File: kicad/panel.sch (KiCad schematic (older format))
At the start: 12 parts, among them CON21 CON5x2, CON22 CON5x2, SW1 SW_PUSH

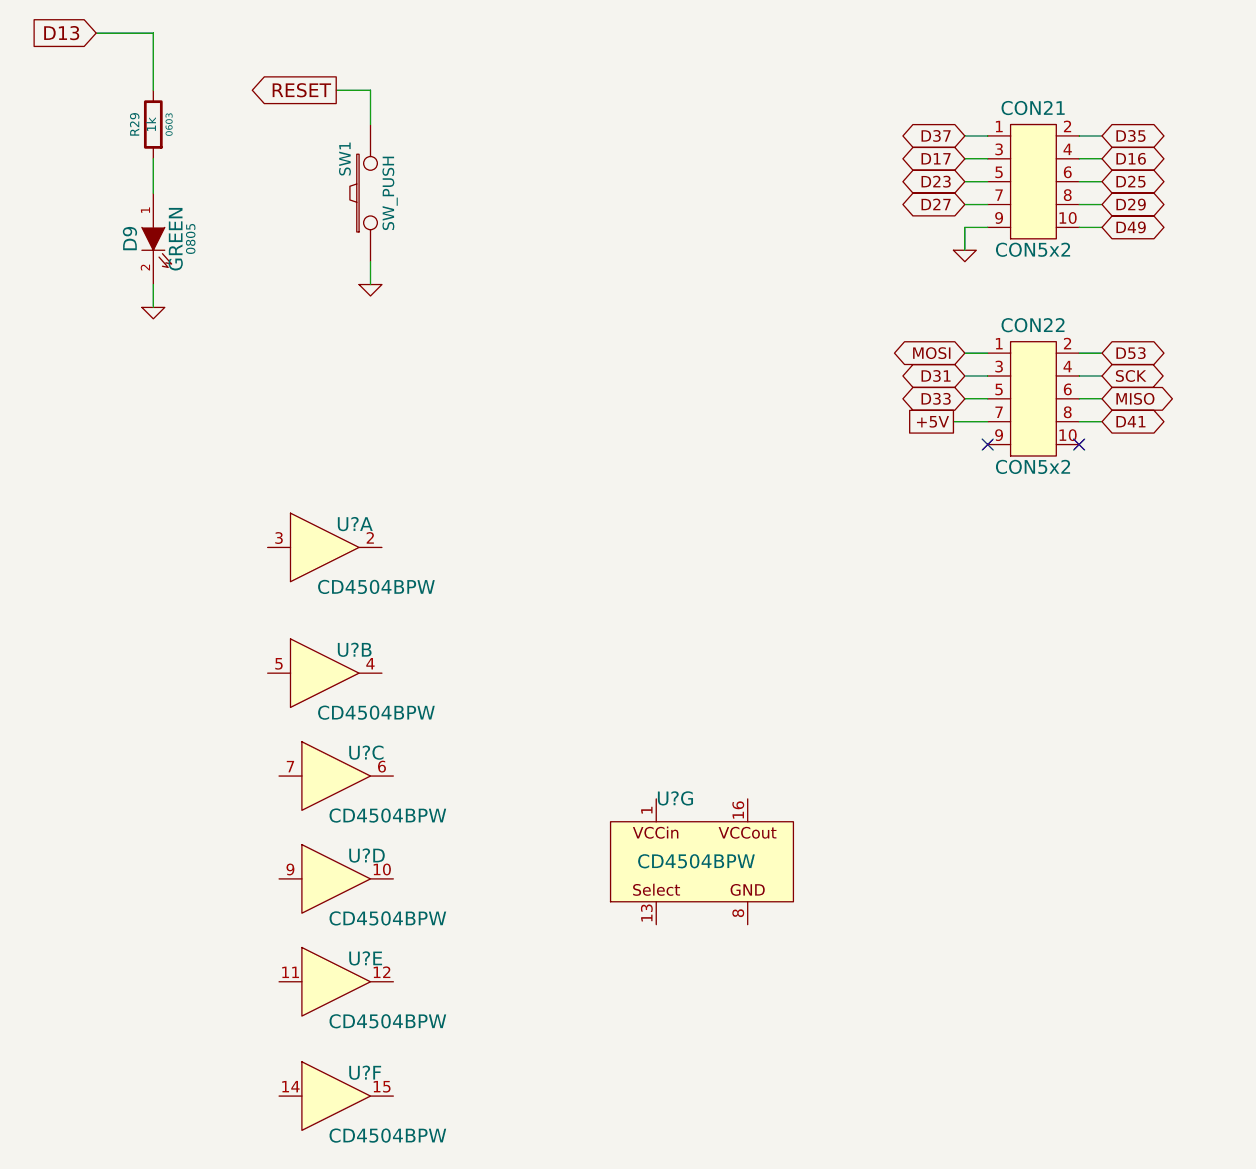
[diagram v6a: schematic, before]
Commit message: Add translators for LCD
ref #11
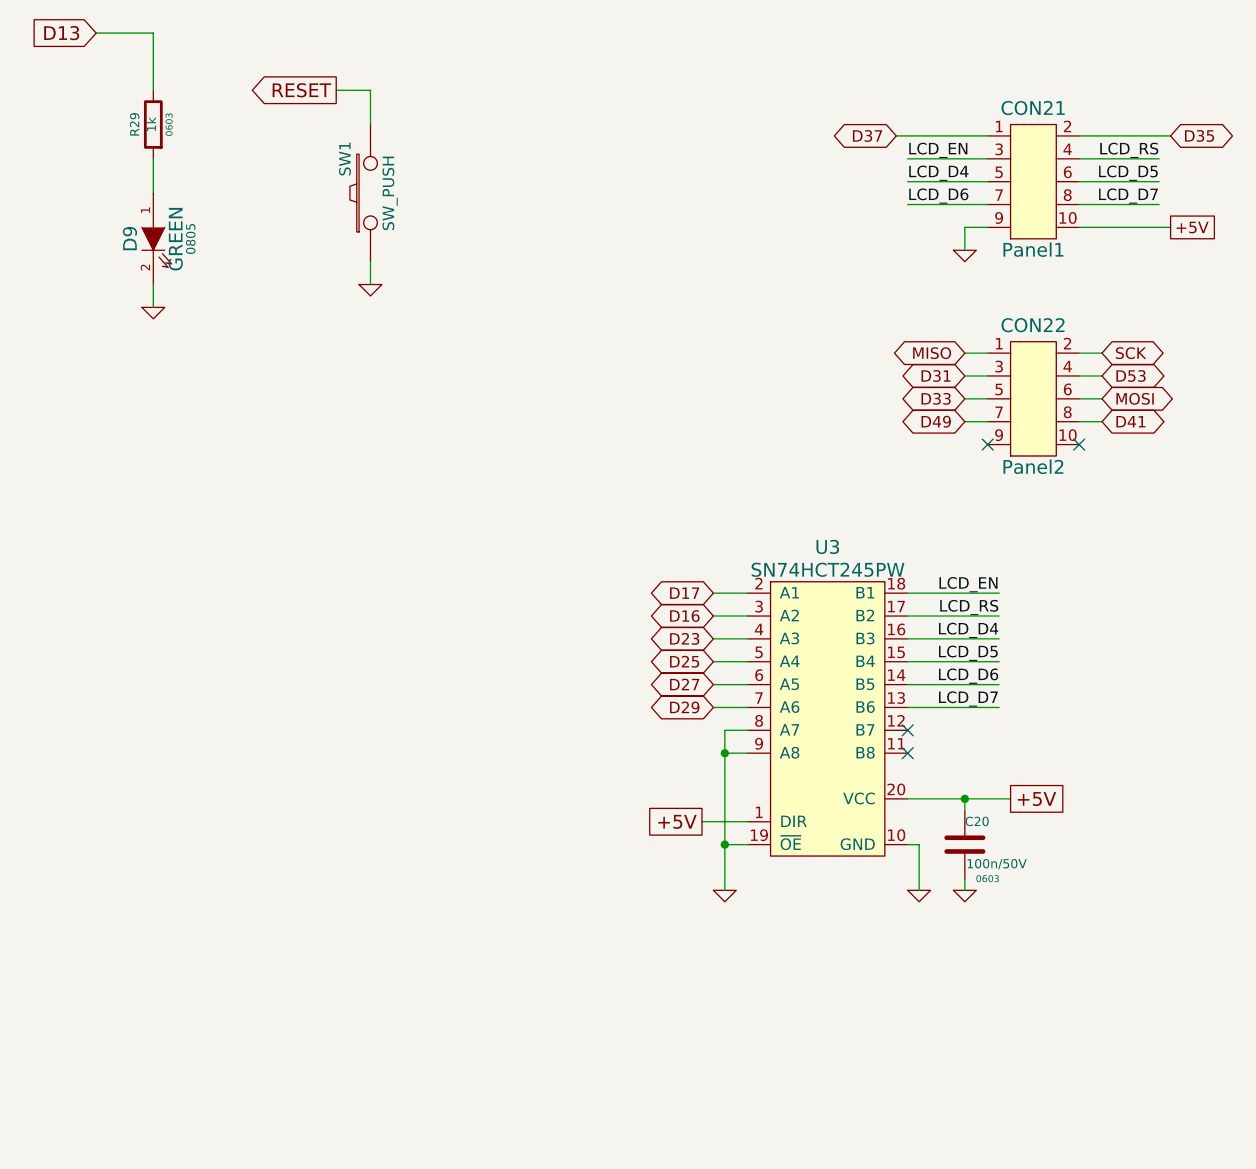
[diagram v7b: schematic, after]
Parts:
- removed U? (x7): CD4504BPW, TSSOP16, symbol CD4504BPW
- added C20: 100n/50V, 0603, symbol C
- added U3: SN74HCT245PW, symbol SN74HCT245PW
- CON21: value CON5x2 -> Panel1
- CON22: value CON5x2 -> Panel2
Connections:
- net +5V: now also CON21.10, C20.1, U3.1 (DIR), U3.20 (VCC); no longer CON22.7
- net D16: now also U3.3 (A2); no longer CON21.4
- net D17: now also U3.2 (A1); no longer CON21.3
- net D23: now also U3.4 (A3); no longer CON21.5
- net D25: now also U3.5 (A4); no longer CON21.6
- net D27: now also U3.6 (A5); no longer CON21.7
- net D29: now also U3.7 (A6); no longer CON21.8
- net D49: now also CON22.7; no longer CON21.10
- net D53: now also CON22.4; no longer CON22.2
- net GND: now also C20.2, U3.10 (GND), U3.19 (~OE), U3.8 (A7), U3.9 (A8)
- net MISO: now also CON22.1; no longer CON22.6
- net MOSI: now also CON22.6; no longer CON22.1
- net SCK: now also CON22.2; no longer CON22.4
- new net LCD_D4: CON21.5, U3.16 (B3)
- new net LCD_D5: CON21.6, U3.15 (B4)
- new net LCD_D6: CON21.7, U3.14 (B5)
- new net LCD_D7: CON21.8, U3.13 (B6)
- new net LCD_EN: CON21.3, U3.18 (B1)
- new net LCD_RS: CON21.4, U3.17 (B2)
- no-connect marks 2 -> 4
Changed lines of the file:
@@
 	0    -1   1    0
 $EndComp
-Text GLabel 6150 1500 2    50   BiDi ~ 0
+Text GLabel 6450 1500 2    50   BiDi ~ 0
 D35
-Text GLabel 5550 1500 0    50   BiDi ~ 0
+Text GLabel 5250 1500 0    50   BiDi ~ 0
 D37
 $Comp
@@
 P 5850 1700
 F 0 "CON21" H 5850 2020 60  0000 C CNN
-F 1 "CON5x2" H 5850 1400 60  0000 C CNN
+F 1 "Panel1" H 5850 1400 60  0000 C CNN
 F 2 "" H 5850 1700 40  0000 C CNN
 F 3 "" H 5850 1700 40  0000 C CNN
@@
 P 5850 2650
 F 0 "CON22" H 5850 2970 60  0000 C CNN
-F 1 "CON5x2" H 5850 2350 60  0000 C CNN
+F 1 "Panel2" H 5850 2350 60  0000 C CNN
 F 2 "" H 5850 2650 40  0000 C CNN
 F 3 "" H 5850 2650 40  0000 C CNN
@@
 	1    0    0    -1
 $EndComp
-Text GLabel 5550 1600 0    50   BiDi ~ 0
+Text GLabel 4450 3500 0    50   BiDi ~ 0
 D17
-Text GLabel 5550 1700 0    50   BiDi ~ 0
+Text GLabel 4450 3700 0    50   BiDi ~ 0
 D23
-Text GLabel 5550 1800 0    50   BiDi ~ 0
+Text GLabel 4450 3900 0    50   BiDi ~ 0
 D27
-Text GLabel 6150 1600 2    50   BiDi ~ 0
+Text GLabel 4450 3600 0    50   BiDi ~ 0
 D16
-Text GLabel 6150 1700 2    50   BiDi ~ 0
+Text GLabel 4450 3800 0    50   BiDi ~ 0
 D25
-Text GLabel 6150 1800 2    50   BiDi ~ 0
+Text GLabel 4450 4000 0    50   BiDi ~ 0
 D29
-Text GLabel 6150 1900 2    50   BiDi ~ 0
-D49
 Wire Wire Line
 	2000 1750 2000 1600
@@
 	2950 2150 2950 2050
 Wire Wire Line
-	6150 1500 6050 1500
-Wire Wire Line
-	6050 1600 6150 1600
-Wire Wire Line
-	6150 1700 6050 1700
-Wire Wire Line
-	6050 1800 6150 1800
-Wire Wire Line
-	6150 1900 6050 1900
+	6450 1500 6050 1500
+Wire Wire Line
+	6050 1600 6400 1600
+Wire Wire Line
+	6400 1700 6050 1700
+Wire Wire Line
+	6050 1800 6400 1800
+Wire Wire Line
+	6450 1900 6050 1900
 Wire Wire Line
 	5550 1900 5650 1900
 Wire Wire Line
-	5550 1800 5650 1800
-Wire Wire Line
-	5550 1700 5650 1700
-Wire Wire Line
-	5650 1600 5550 1600
-Wire Wire Line
-	5650 1500 5550 1500
+	5300 1800 5650 1800
+Wire Wire Line
+	5300 1700 5650 1700
+Wire Wire Line
+	5650 1600 5300 1600
+Wire Wire Line
+	5650 1500 5250 1500
 $Comp
 L GND #PWR52
@@
 Wire Wire Line
 	5550 1900 5550 2000
-Text GLabel 5550 2450 0    50   BiDi ~ 0
+Text GLabel 6150 2650 2    50   BiDi ~ 0
 MOSI
 Text GLabel 5550 2550 0    50   BiDi ~ 0
@@
 Text GLabel 5550 2650 0    50   BiDi ~ 0
 D33
-Text GLabel 5500 2750 0    50   UnSpc ~ 0
+Text GLabel 6450 1900 2    50   UnSpc ~ 0
 +5V
 Wire Wire Line
-	5500 2750 5650 2750
+	5550 2750 5650 2750
 Wire Wire Line
 	5550 2650 5650 2650
@@
 Wire Wire Line
 	5650 2450 5550 2450
+Text GLabel 6150 2550 2    50   BiDi ~ 0
+D53
 Text GLabel 6150 2450 2    50   BiDi ~ 0
-D53
-Text GLabel 6150 2550 2    50   BiDi ~ 0
 SCK
-Text GLabel 6150 2650 2    50   BiDi ~ 0
+Text GLabel 5550 2450 0    50   BiDi ~ 0
 MISO
 Text GLabel 6150 2750 2    50   BiDi ~ 0
@@
 NoConn ~ 6050 2850
 NoConn ~ 5650 2850
-$Comp
-L CD4504BPW U?
-U 1 1 538D7C6B
-P 2750 3300
-F 0 "U?" H 2800 3400 60  0000 L CNN
-F 1 "CD4504BPW" H 2975 3125 60  0000 C CNN
-F 2 "TSSOP16" H 2625 3300 40  0001 L CNN
-F 3 "" H 2600 3900 60  0001 L CNN
-	1    2750 3300
-	1    0    0    -1
-$EndComp
-$Comp
-L CD4504BPW U?
-U 2 1 538D7CB8
-P 2750 3850
-F 0 "U?" H 2800 3950 60  0000 L CNN
-F 1 "CD4504BPW" H 2975 3675 60  0000 C CNN
-F 2 "TSSOP16" H 2625 3850 40  0001 L CNN
-F 3 "" H 2600 4450 60  0001 L CNN
-	2    2750 3850
-	1    0    0    -1
-$EndComp
-$Comp
-L CD4504BPW U?
-U 3 1 538D7D0D
-P 2800 4300
-F 0 "U?" H 2850 4400 60  0000 L CNN
-F 1 "CD4504BPW" H 3025 4125 60  0000 C CNN
-F 2 "TSSOP16" H 2675 4300 40  0001 L CNN
-F 3 "" H 2650 4900 60  0001 L CNN
-	3    2800 4300
-	1    0    0    -1
-$EndComp
-$Comp
-L CD4504BPW U?
-U 4 1 538D7D48
-P 2800 4750
-F 0 "U?" H 2850 4850 60  0000 L CNN
-F 1 "CD4504BPW" H 3025 4575 60  0000 C CNN
-F 2 "TSSOP16" H 2675 4750 40  0001 L CNN
-F 3 "" H 2650 5350 60  0001 L CNN
-	4    2800 4750
-	1    0    0    -1
-$EndComp
-$Comp
-L CD4504BPW U?
-U 5 1 538D7D79
-P 2800 5200
-F 0 "U?" H 2850 5300 60  0000 L CNN
-F 1 "CD4504BPW" H 3025 5025 60  0000 C CNN
-F 2 "TSSOP16" H 2675 5200 40  0001 L CNN
-F 3 "" H 2650 5800 60  0001 L CNN
-	5    2800 5200
-	1    0    0    -1
-$EndComp
-$Comp
-L CD4504BPW U?
-U 6 1 538D7DA4
-P 2800 5700
-F 0 "U?" H 2850 5800 60  0000 L CNN
-F 1 "CD4504BPW" H 3025 5525 60  0000 C CNN
-F 2 "TSSOP16" H 2675 5700 40  0001 L CNN
-F 3 "" H 2650 6300 60  0001 L CNN
-	6    2800 5700
-	1    0    0    -1
-$EndComp
-$Comp
-L CD4504BPW U?
-U 7 1 538D7DD3
-P 4150 4500
-F 0 "U?" H 4200 4600 60  0000 L CNN
-F 1 "CD4504BPW" H 4375 4325 60  0000 C CNN
-F 2 "TSSOP16" H 4025 4500 40  0001 L CNN
-F 3 "" H 4000 5100 60  0001 L CNN
-	7    4150 4500
-	1    0    0    -1
-$EndComp
+Text GLabel 5550 2750 0    50   BiDi ~ 0
+D49
+$Comp
+L SN74HCT245PW U3
+U 1 1 538E2F48
+P 4950 3850
+F 0 "U3" H 4950 4400 60  0000 C CNN
+F 1 "SN74HCT245PW" H 4950 4300 60  0000 C CNN
+F 2 "" H 4950 4350 60  0000 C CNN
+F 3 "" H 4950 4350 60  0000 C CNN
+	1    4950 3850
+	1    0    0    -1
+$EndComp
+$Comp
+L C C20
+U 1 1 538E32B7
+P 5550 4600
+F 0 "C20" H 5550 4700 40  0000 L CNN
+F 1 "100n/50V" H 5556 4515 40  0000 L CNN
+F 2 "0603" H 5650 4450 30  0000 C CNN
+F 3 "" H 5550 4600 60  0000 C CNN
+	1    5550 4600
+	1    0    0    -1
+$EndComp
+$Comp
+L GND #PWR57
+U 1 1 538E32BE
+P 5550 4800
+F 0 "#PWR57" H 5550 4800 30  0001 C CNN
+F 1 "GND" H 5550 4730 30  0001 C CNN
+F 2 "" H 5550 4800 60  0000 C CNN
+F 3 "" H 5550 4800 60  0000 C CNN
+	1    5550 4800
+	1    0    0    -1
+$EndComp
+Wire Wire Line
+	5550 4400 5550 4450
+Wire Wire Line
+	5550 4750 5550 4800
+Wire Wire Line
+	5300 4400 5750 4400
+$Comp
+L GND #PWR56
+U 1 1 538E3349
+P 5350 4800
+F 0 "#PWR56" H 5350 4800 30  0001 C CNN
+F 1 "GND" H 5350 4730 30  0001 C CNN
+F 2 "" H 5350 4800 60  0000 C CNN
+F 3 "" H 5350 4800 60  0000 C CNN
+	1    5350 4800
+	1    0    0    -1
+$EndComp
+Wire Wire Line
+	5350 4800 5350 4600
+Wire Wire Line
+	5350 4600 5300 4600
+Text GLabel 5750 4400 2    60   UnSpc ~ 0
++5V
+Connection ~ 5550 4400
+Text GLabel 4400 4500 0    60   UnSpc ~ 0
++5V
+Wire Wire Line
+	4600 4500 4400 4500
+$Comp
+L GND #PWR55
+U 1 1 538E301C
+P 4500 4800
+F 0 "#PWR55" H 4500 4800 30  0001 C CNN
+F 1 "GND" H 4500 4730 30  0001 C CNN
+F 2 "" H 4500 4800 60  0000 C CNN
+F 3 "" H 4500 4800 60  0000 C CNN
+	1    4500 4800
+	1    0    0    -1
+$EndComp
+Wire Wire Line
+	4500 4100 4500 4800
+Wire Wire Line
+	4500 4600 4600 4600
+Wire Wire Line
+	4450 3500 4600 3500
+Wire Wire Line
+	4450 3600 4600 3600
+Wire Wire Line
+	4450 3700 4600 3700
+Wire Wire Line
+	4450 3800 4600 3800
+Wire Wire Line
+	4450 3900 4600 3900
+Wire Wire Line
+	4450 4000 4600 4000
+Text Label 5300 1600 0    50   ~ 0
+LCD_EN
+Text Label 5300 1700 0    50   ~ 0
+LCD_D4
+Text Label 5300 1800 0    50   ~ 0
+LCD_D6
+Text Label 6400 1600 2    50   ~ 0
+LCD_RS
+Text Label 6400 1700 2    50   ~ 0
+LCD_D5
+Text Label 6400 1800 2    50   ~ 0
+LCD_D7
+Text Label 5700 3500 2    50   ~ 0
+LCD_EN
+Text Label 5700 3700 2    50   ~ 0
+LCD_D4
+Text Label 5700 3900 2    50   ~ 0
+LCD_D6
+Text Label 5700 3600 2    50   ~ 0
+LCD_RS
+Text Label 5700 3800 2    50   ~ 0
+LCD_D5
+Text Label 5700 4000 2    50   ~ 0
+LCD_D7
+Wire Wire Line
+	5300 3500 5700 3500
+Wire Wire Line
+	5700 3600 5300 3600
+Wire Wire Line
+	5300 3700 5700 3700
+Wire Wire Line
+	5700 3800 5300 3800
+Wire Wire Line
+	5300 3900 5700 3900
+Wire Wire Line
+	5700 4000 5300 4000
+Wire Wire Line
+	4600 4100 4500 4100
+Connection ~ 4500 4600
+Wire Wire Line
+	4600 4200 4500 4200
+Connection ~ 4500 4200
+NoConn ~ 5300 4100
+NoConn ~ 5300 4200
 $EndSCHEMATC
